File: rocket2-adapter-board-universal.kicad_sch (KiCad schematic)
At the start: 13 parts, among them J2 Conn_01x04_Socket, J3 Conn_01x02_Socket, J4 Conn_01x04_Socket, J5 DSUB_15pin/VGA Veritical Fema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

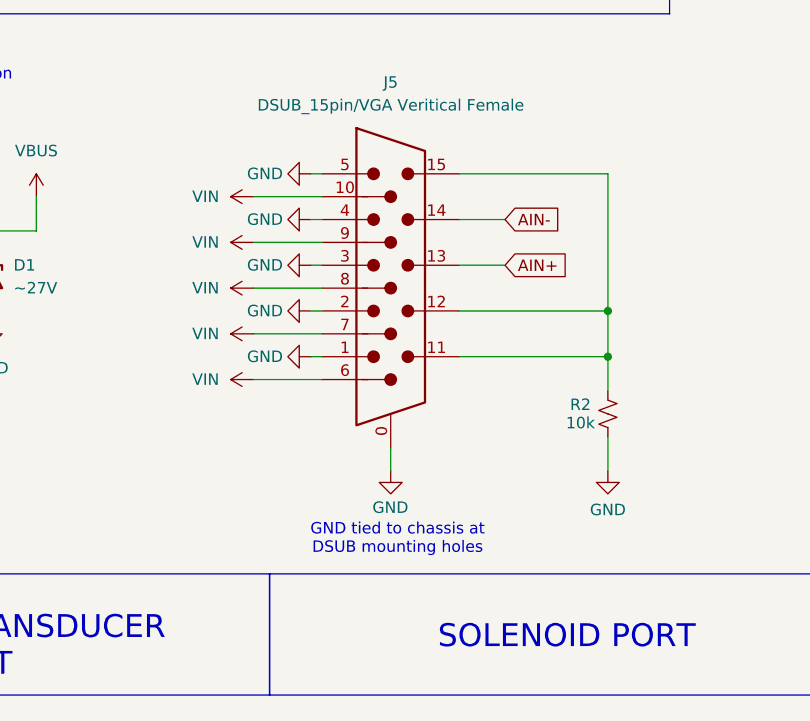
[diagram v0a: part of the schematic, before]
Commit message: Layout Update 2 + DSUB & Footprint Fixes
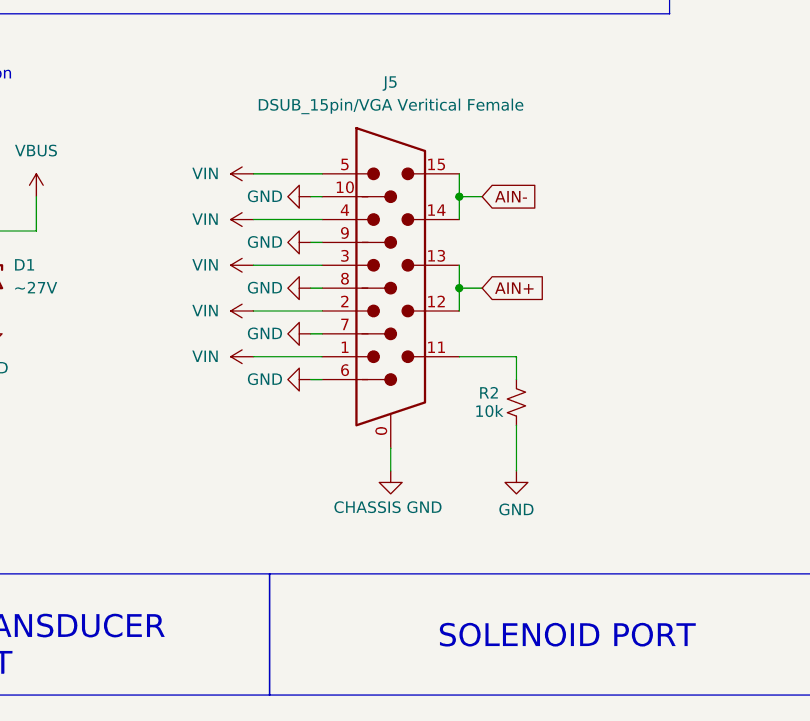
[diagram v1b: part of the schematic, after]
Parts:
- D1: footprint Diode_SMD:D_0603_1608Metric -> Diode_SMD:D_SOD-123
- F1: footprint Fuse:Fuse_0603_1608Metric -> Fuse:Fuseholder_Blade_Mini_Keystone_3568
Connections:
- net AIN+: now also J5.12
- net AIN-: now also J5.15
- net GND: now also J5.10, J5.6, J5.7, J5.8, J5.9; no longer J5.0, J5.1, J5.2, J5.3, J5.4, J5.5
- net VIN: now also J5.1, J5.2, J5.3, J5.4, J5.5; no longer J5.10, J5.6, J5.7, J5.8, J5.9
- net at J5.11, R2.2: no longer J5.12, J5.15
- new net CHASSIS GND: J5.0
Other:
- note removed: "GND tied to chassis at DSUB mounting holes"
- moved on the sheet: R2

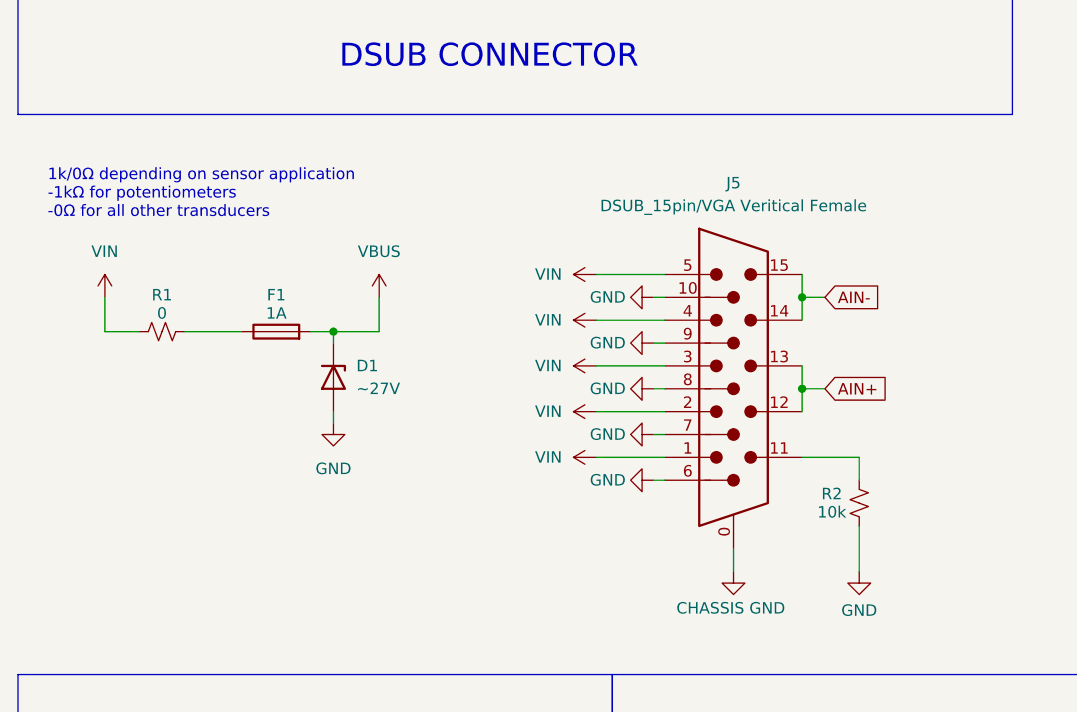
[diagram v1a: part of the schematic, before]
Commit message: Layout Update 3 + Schematic Links & DSUB Update
Added R2 to bridge AIN+ and AIN-
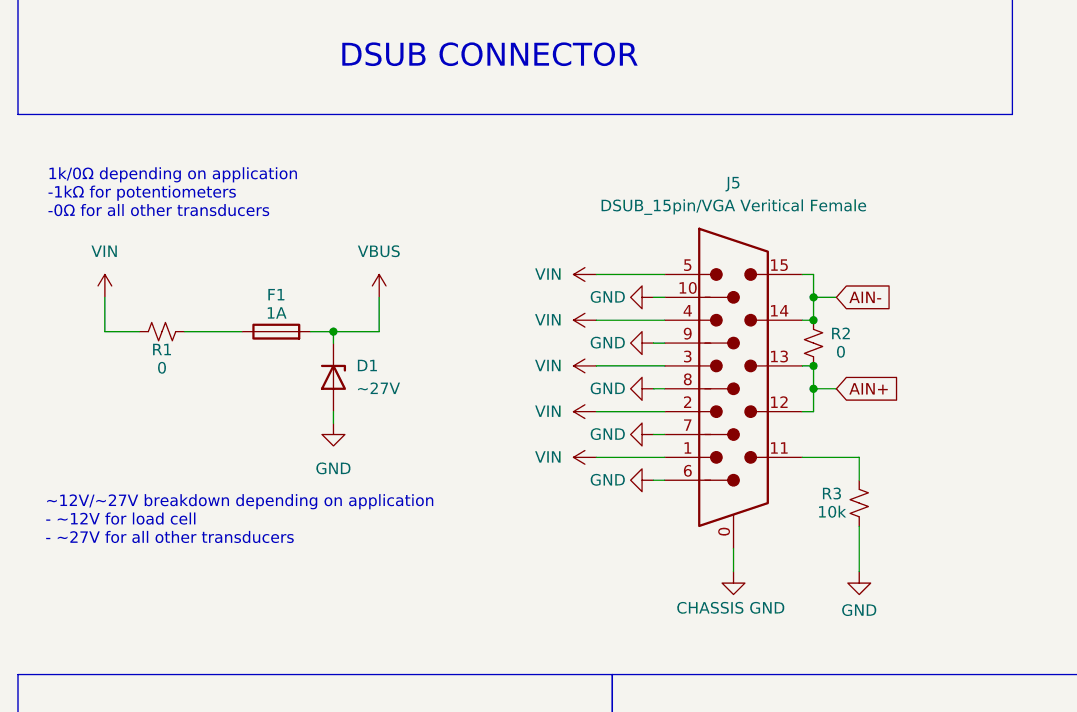
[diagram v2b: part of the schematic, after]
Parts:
- added R2: 0, Resistor_SMD:R_0603_1608Metric, symbol Device:R_Small_US
- D1: Alt. Digikey Link (none) -> https://www.digikey.com/en/products/detail/diodes-incorpora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; Alt. MPN (none) -> BZT52C12-13-F; Alt. Manufacturer (none) -> Diodes Incorporated
- R1: Alt. Digikey Link (none) -> SR0603JR-7T1KL; Alt. MPN (none) -> https://www.digikey.com/en/products/detail/yageo/SR0603JR-7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; Alt. Manufacturer (none) -> YAGEO; MPN (none) -> 0603WAJ0000T5E; Manufacturer (none) -> UNI-ROYAL
- R3: renamed from R2; MPN (none) -> 0603WAJ0103T5E; Manufacturer (none) -> UNI-ROYAL
- VR1: Digikey Link (none) -> https://www.digikey.com/en/products/detail/tt-electronics-b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; MPN P160KNPD -4FC20B10K -> P160KNPD-4FC20B10K; Supplier https://www.digikey.com/en/products/detail/tt-electronics-b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 -> (none)
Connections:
- net AIN+: now also R2.2
- net AIN-: now also R2.1
- net VIN: now also R1.2; no longer R1.1
- net at F1.1: now also R1.1; no longer R1.2
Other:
- note added: "1k/0Ω depending on application -1kΩ for potentiometers -0Ω for all other transducers"
- note added: "~12V/~27V breakdown depending on application - ~12V for load cell - ~27V for all other transducers"
- note removed: "1k/0Ω depending on sensor application -1kΩ for potentiometers -0Ω for all other transducers"
- moved on the sheet: R1

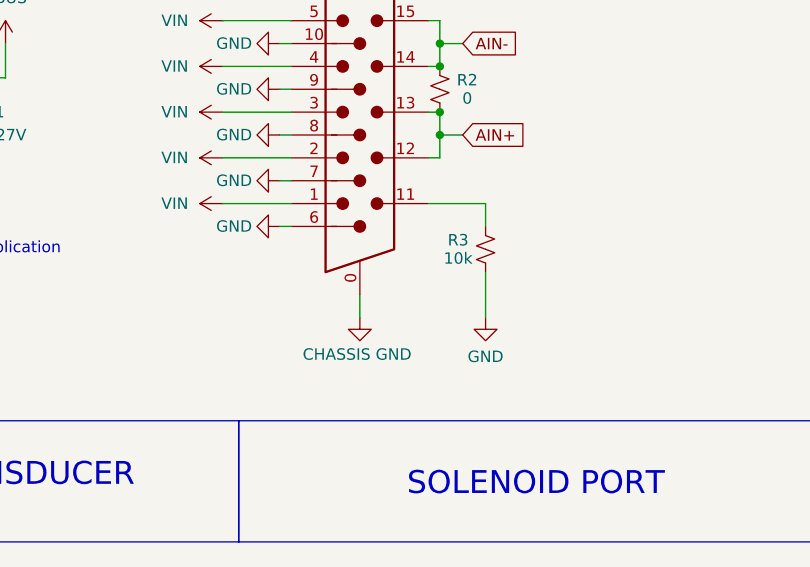
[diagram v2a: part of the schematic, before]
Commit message: Layout Update 4: NC pins, PT and Solenoid pad fixes
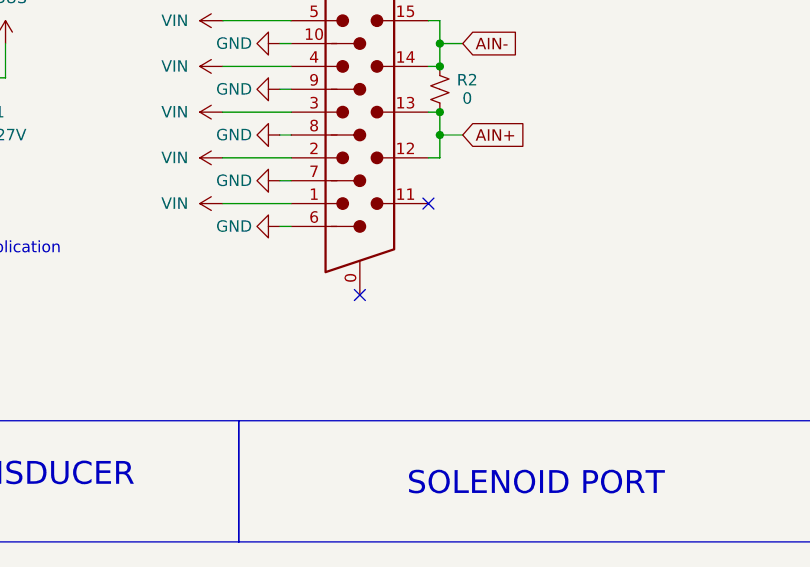
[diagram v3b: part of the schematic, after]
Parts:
- removed R3: 10k, Resistor_SMD:R_0603_1608Metric, symbol Device:R_Small_US
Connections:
- net CHASSIS GND: no longer names the net of J5.0
- no-connect marks 1 -> 3

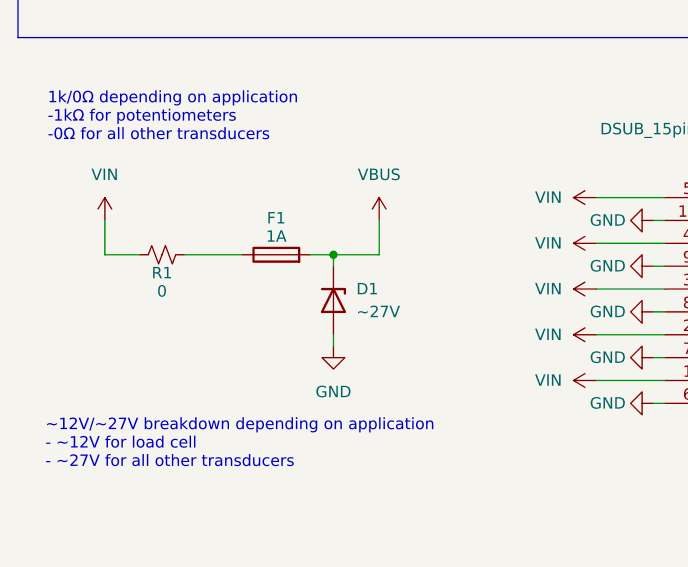
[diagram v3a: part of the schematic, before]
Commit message: Layout Update 5: Part spacing, Footprints, and Models
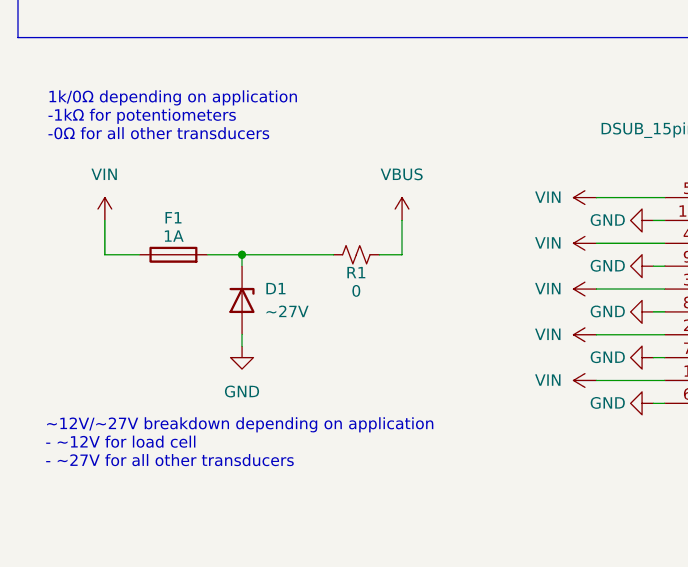
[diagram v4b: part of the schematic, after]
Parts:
- J3: footprint Connector_PinHeader_2.54mm:PinHeader_1x02_P2.54mm_Vertical -> UCIRP-KiCAD-Lib:Pad_Socket 16AWG_Solenoid_Wires
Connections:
- net VBUS: now also R1.1; no longer D1.1 (K), F1.2
- net VIN: now also F1.1; no longer R1.2
- new net: D1.1 (K), F1.2, R1.2
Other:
- moved on the sheet: D1, F1, R1
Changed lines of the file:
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@@
+	)
+	(junction
+		(at 36.83 49.53)
+		(diameter 0)
+		(color 0 0 0 0)
 	)
 	(junction
@@
 	)
 	(junction
-		(at 46.99 49.53)
-		(diameter 0)
-		(color 0 0 0 0)
-	)
-	(junction
 		(at 100.33 55.88)
 		(diameter 0)
@@
 	(wire
 		(pts
+			(xy 33.02 49.53) (xy 36.83 49.53)
+		)
+		(stroke
+			(width 0)
+			(type default)
+		)
+	)
+	(wire
+		(pts
 			(xy 99.06 118.11) (xy 99.06 115.57)
 		)
@@
 	(wire
 		(pts
-			(xy 46.99 50.8) (xy 46.99 49.53)
-		)
-		(stroke
-			(width 0)
-			(type default)
-		)
-	)
-	(wire
-		(pts
 			(xy 99.06 123.19) (xy 99.06 120.65)
 		)
@@
 	(wire
 		(pts
-			(xy 46.99 59.69) (xy 46.99 58.42)
+			(xy 36.83 59.69) (xy 36.83 58.42)
 		)
 		(stroke
@@
 	(wire
 		(pts
-			(xy 46.99 49.53) (xy 52.07 49.53)
-		)
-		(stroke
-			(width 0)
-			(type default)
-		)
-	)
-	(wire
-		(pts
-			(xy 52.07 45.72) (xy 52.07 49.53)
+			(xy 54.61 45.72) (xy 54.61 49.53)
 		)
 		(stroke
@@
 	(wire
 		(pts
+			(xy 36.83 49.53) (xy 46.99 49.53)
+		)
+		(stroke
+			(width 0)
+			(type default)
+		)
+	)
+	(wire
+		(pts
+			(xy 52.07 49.53) (xy 54.61 49.53)
+		)
+		(stroke
+			(width 0)
+			(type default)
+		)
+	)
+	(wire
+		(pts
+			(xy 36.83 49.53) (xy 36.83 50.8)
+		)
+		(stroke
+			(width 0)
+			(type default)
+		)
+	)
+	(wire
+		(pts
 			(xy 82.55 60.96) (xy 83.82 60.96)
 		)
@@
 	(wire
 		(pts
-			(xy 30.48 49.53) (xy 36.83 49.53)
-		)
-		(stroke
-			(width 0)
-			(type default)
-		)
-	)
-	(wire
-		(pts
 			(xy 82.55 66.04) (xy 83.82 66.04)
 		)
@@
 		(pts
 			(xy 100.33 55.88) (xy 102.87 55.88)
-		)
-		(stroke
-			(width 0)
-			(type default)
-		)
-	)
-	(wire
-		(pts
-			(xy 44.45 49.53) (xy 46.99 49.53)
 		)
 		(stroke
@@
 	(symbol
 		(lib_id "Device:Fuse")
-		(at 40.64 49.53 90)
+		(at 29.21 49.53 90)
 		(unit 1)
 		(exclude_from_sim no)
@@
 		(dnp no)
 		(property "Reference" "F1"
-			(at 40.64 45.466 90)
+			(at 29.21 45.466 90)
 			(effects
 				(font
@@
 		)
 		(property "Value" "1A"
-			(at 40.64 47.498 90)
+			(at 29.21 47.498 90)
 			(effects
 				(font
@@
 		)
 		(property "Footprint" "Fuse:Fuseholder_Blade_Mini_Keystone_3568"
-			(at 40.64 51.308 90)
+			(at 29.21 51.308 90)
 			(effects
 				(font
@@
 		)
 		(property "Datasheet" "https://jlcpcb.com/partdetail/Keystone-3568/C5249699"
-			(at 40.64 49.53 0)
+			(at 29.21 49.53 0)
 			(effects
 				(font
@@
 		)
 		(property "Description" "Fuse"
-			(at 40.64 49.53 0)
+			(at 29.21 49.53 0)
 			(effects
 				(font
@@
 	(symbol
 		(lib_id "Device:D_Zener")
-		(at 46.99 54.61 270)
+		(at 36.83 54.61 270)
 		(unit 1)
 		(exclude_from_sim no)
@@
 		(fields_autoplaced yes)
 		(property "Reference" "D1"
-			(at 49.53 53.3399 90)
+			(at 39.37 53.3399 90)
 			(effects
 				(font
@@
 		)
 		(property "Value" "~27V"
-			(at 49.53 55.8799 90)
+			(at 39.37 55.8799 90)
 			(effects
 				(font
@@
 		)
 		(property "Footprint" "Diode_SMD:D_SOD-123"
-			(at 46.99 54.61 0)
+			(at 36.83 54.61 0)
 			(effects
 				(font
@@
 		)
 		(property "Datasheet" "https://jlcpcb.com/partdetail/DiodesIncorporated-MMSZ5254BQ_7F/C6909633"
-			(at 46.99 54.61 0)
+			(at 36.83 54.61 0)
 			(effects
 				(font
@@
 		)
 		(property "Description" "Zener diode"
-			(at 46.99 54.61 0)
+			(at 36.83 54.61 0)
 			(effects
 				(font
@@
 		)
 		(property "Alt. Digikey Link" "https://www.digikey.com/en/products/detail/diodes-incorporated/BZT52C12-13-F/768854"
-			(at 46.99 54.61 90)
+			(at 36.83 54.61 90)
 			(effects
 				(font
@@
 		)
 		(property "Alt. MPN" "BZT52C12-13-F"
-			(at 46.99 54.61 90)
+			(at 36.83 54.61 90)
 			(effects
 				(font
@@
 		)
 		(property "Alt. Manufacturer" "Diodes Incorporated"
-			(at 46.99 54.61 90)
+			(at 36.83 54.61 90)
 			(effects
 				(font
@@
 	(symbol
 		(lib_id "power:VD")
-		(at 52.07 45.72 0)
+		(at 54.61 45.72 0)
 		(unit 1)
 		(exclude_from_sim no)
@@
 		(dnp no)
 		(property "Reference" "#PWR04"
-			(at 52.07 49.53 0)
+			(at 54.61 49.53 0)
 			(effects
 				(font
@@
 		)
 		(property "Value" "VBUS"
-			(at 52.07 40.64 0)
+			(at 54.61 40.64 0)
 			(effects
 				(font
@@
 		)
 		(property "Footprint" ""
-			(at 52.07 45.72 0)
+			(at 54.61 45.72 0)
 			(effects
 				(font
@@
 		)
 		(property "Datasheet" ""
-			(at 52.07 45.72 0)
+			(at 54.61 45.72 0)
 			(effects
 				(font
@@
 		)
 		(property "Description" "Power symbol creates a global label with name \"VD\""
-			(at 52.07 45.72 0)
+			(at 54.61 45.72 0)
 			(effects
 				(font
@@
 	(symbol
 		(lib_id "Device:R_Small_US")
-		(at 27.94 49.53 270)
+		(at 49.53 49.53 270)
 		(unit 1)
 		(exclude_from_sim no)
@@
 		(dnp no)
 		(property "Reference" "R1"
-			(at 27.94 51.562 90)
+			(at 49.53 51.562 90)
 			(effects
 				(font
@@
 		)
 		(property "Value" "0"
-			(at 27.94 53.594 90)
+			(at 49.53 53.594 90)
 			(effects
 				(font
@@
 		)
 		(property "Footprint" "Resistor_SMD:R_0603_1608Metric"
-			(at 27.94 49.53 0)
+			(at 49.53 49.53 0)
 			(effects
 				(font
@@
 		)
 		(property "Datasheet" "https://jlcpcb.com/partdetail/16080-0603WAJ0000T5E/C15402"
-			(at 27.94 49.53 0)
+			(at 49.53 49.53 0)
 			(effects
 				(font
@@
 		)
 		(property "Description" "Resistor, small US symbol"
-			(at 27.94 49.53 0)
+			(at 49.53 49.53 0)
 			(effects
 				(font
@@
 		)
 		(property "MPN" "0603WAJ0000T5E"
-			(at 27.94 49.53 90)
+			(at 49.53 49.53 90)
 			(effects
 				(font
@@
 		)
 		(property "Manufacturer" "UNI-ROYAL"
-			(at 27.94 49.53 90)
+			(at 49.53 49.53 90)
 			(effects
 				(font
@@
 		)
 		(property "Alt. Digikey Link" "SR0603JR-7T1KL"
-			(at 27.94 49.53 90)
+			(at 49.53 49.53 90)
 			(effects
 				(font
@@
 		)
 		(property "Alt. MPN" "https://www.digikey.com/en/products/detail/yageo/SR0603JR-7T1KL/9696404"
-			(at 27.94 49.53 90)
+			(at 49.53 49.53 90)
 			(effects
 				(font
@@
 		)
 		(property "Alt. Manufacturer" "YAGEO"
-			(at 27.94 49.53 90)
+			(at 49.53 49.53 90)
 			(effects
 				(font
@@
 			)
 		)
-		(property "Footprint" "Connector_PinHeader_2.54mm:PinHeader_1x02_P2.54mm_Vertical"
+		(property "Footprint" "UCIRP-KiCAD-Lib:Pad_Socket 16AWG_Solenoid_Wires"
 			(at 107.95 118.11 0)
 			(effects
@@
 	(symbol
 		(lib_id "power:GND")
-		(at 46.99 59.69 0)
+		(at 36.83 59.69 0)
 		(mirror y)
 		(unit 1)
@@
 		(dnp no)
 		(property "Reference" "#PWR015"
-			(at 46.99 66.04 0)
+			(at 36.83 66.04 0)
 			(effects
 				(font
@@
 		)
 		(property "Value" "GND"
-			(at 46.99 64.77 0)
+			(at 36.83 64.77 0)
 			(effects
 				(font
@@
 		)
 		(property "Footprint" ""
-			(at 46.99 59.69 0)
+			(at 36.83 59.69 0)
 			(effects
 				(font
@@
 		)
 		(property "Datasheet" ""
-			(at 46.99 59.69 0)
+			(at 36.83 59.69 0)
 			(effects
 				(font
@@
 		)
 		(property "Description" "Power symbol creates a global label with name \"GND\" , ground"
-			(at 46.99 59.69 0)
-			(effects
-				(font
+			(at 36.83 59.69 0)
+			(effects
+				(font

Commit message: Layout Update 6: Updated PT footprint, Silkscreen labels, M3s
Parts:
- H1, H2, H3, H4: footprint MountingHole:MountingHole_4.3mm_M4_ISO7380_Pad -> MountingHole:MountingHole_3.2mm_M3_ISO7380
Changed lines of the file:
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@@
 			)
 		)
-		(property "Footprint" "MountingHole:MountingHole_4.3mm_M4_ISO7380_Pad"
+		(property "Footprint" "MountingHole:MountingHole_3.2mm_M3_ISO7380"
 			(at 59.69 156.21 0)
 			(effects
@@
 			)
 		)
-		(property "Footprint" "MountingHole:MountingHole_4.3mm_M4_ISO7380_Pad"
+		(property "Footprint" "MountingHole:MountingHole_3.2mm_M3_ISO7380"
 			(at 59.69 172.72 0)
 			(effects
@@
 			)
 		)
-		(property "Footprint" "MountingHole:MountingHole_4.3mm_M4_ISO7380_Pad"
+		(property "Footprint" "MountingHole:MountingHole_3.2mm_M3_ISO7380"
 			(at 25.4 156.21 0)
 			(effects
@@
 			)
 		)
-		(property "Footprint" "MountingHole:MountingHole_4.3mm_M4_ISO7380_Pad"
+		(property "Footprint" "MountingHole:MountingHole_3.2mm_M3_ISO7380"
 			(at 25.4 172.72 0)
 			(effects

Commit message: Ready for purchasing
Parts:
- H1: footprint MountingHole:MountingHole_3.2mm_M3_ISO7380 -> MountingHole:MountingHole_3.2mm_M3_DIN965_Pad
- H2, H3, H4: footprint MountingHole:MountingHole_3.2mm_M3_ISO7380 -> MountingHole:MountingHole_3.2mm_M3_ISO7380_Pad
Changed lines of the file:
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@@
 		)
 		(instances
-			(project ""
+			(project "rocket2-adapter-board-universal"
 				(path "/ebb2d496-aa62-4c9f-aa1f-c2b6bd418c17"
 					(reference "F1")
@@
 		)
 		(instances
-			(project ""
+			(project "rocket2-adapter-board-universal"
 				(path "/ebb2d496-aa62-4c9f-aa1f-c2b6bd418c17"
 					(reference "D1")
@@
 		)
 		(instances
-			(project ""
+			(project "rocket2-adapter-board-universal"
 				(path "/ebb2d496-aa62-4c9f-aa1f-c2b6bd418c17"
 					(reference "VR1")
@@
 			)
 		)
-		(property "Footprint" "MountingHole:MountingHole_3.2mm_M3_ISO7380"
+		(property "Footprint" "MountingHole:MountingHole_3.2mm_M3_ISO7380_Pad"
 			(at 59.69 156.21 0)
 			(effects
@@
 		)
 		(instances
-			(project ""
+			(project "rocket2-adapter-board-universal"
 				(path "/ebb2d496-aa62-4c9f-aa1f-c2b6bd418c17"
 					(reference "J5")
@@
 			)
 		)
-		(property "Footprint" "MountingHole:MountingHole_3.2mm_M3_ISO7380"
+		(property "Footprint" "MountingHole:MountingHole_3.2mm_M3_ISO7380_Pad"
 			(at 59.69 172.72 0)
 			(effects
@@
 		)
 		(instances
-			(project "rocket2-adapter-board-load-cell"
+			(project "rocket2-adapter-board-universal"
 				(path "/ebb2d496-aa62-4c9f-aa1f-c2b6bd418c17"
 					(reference "#PWR05")
@@
 		)
 		(instances
-			(project ""
+			(project "rocket2-adapter-board-universal"
 				(path "/ebb2d496-aa62-4c9f-aa1f-c2b6bd418c17"
 					(reference "J3")
@@
 			)
 		)
-		(property "Footprint" "MountingHole:MountingHole_3.2mm_M3_ISO7380"
+		(property "Footprint" "MountingHole:MountingHole_3.2mm_M3_DIN965_Pad"
 			(at 25.4 156.21 0)
 			(effects
@@
 		)
 		(instances
-			(project ""
+			(project "rocket2-adapter-board-universal"
 				(path "/ebb2d496-aa62-4c9f-aa1f-c2b6bd418c17"
 					(reference "H1")
@@
 			)
 		)
-		(property "Footprint" "MountingHole:MountingHole_3.2mm_M3_ISO7380"
+		(property "Footprint" "MountingHole:MountingHole_3.2mm_M3_ISO7380_Pad"
 			(at 25.4 172.72 0)
 			(effects
